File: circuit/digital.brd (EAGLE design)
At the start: 56.2 x 50.8 mm, 24 parts, among them IC1 MCP1701-5V, IC2 MCP1700-3.3V, X1 MINI-USB-SCHIELD-32005-301

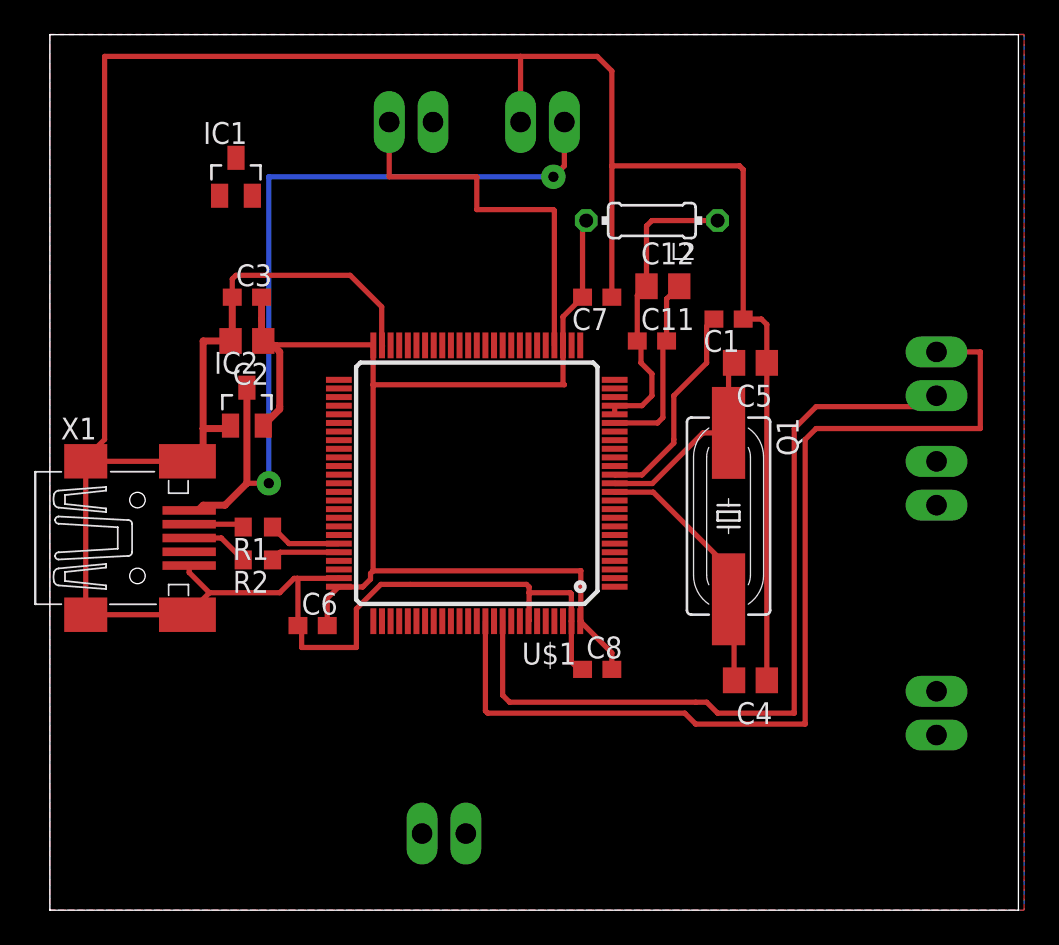
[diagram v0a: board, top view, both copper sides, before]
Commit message: - развели все пины идущие к аналоговой части
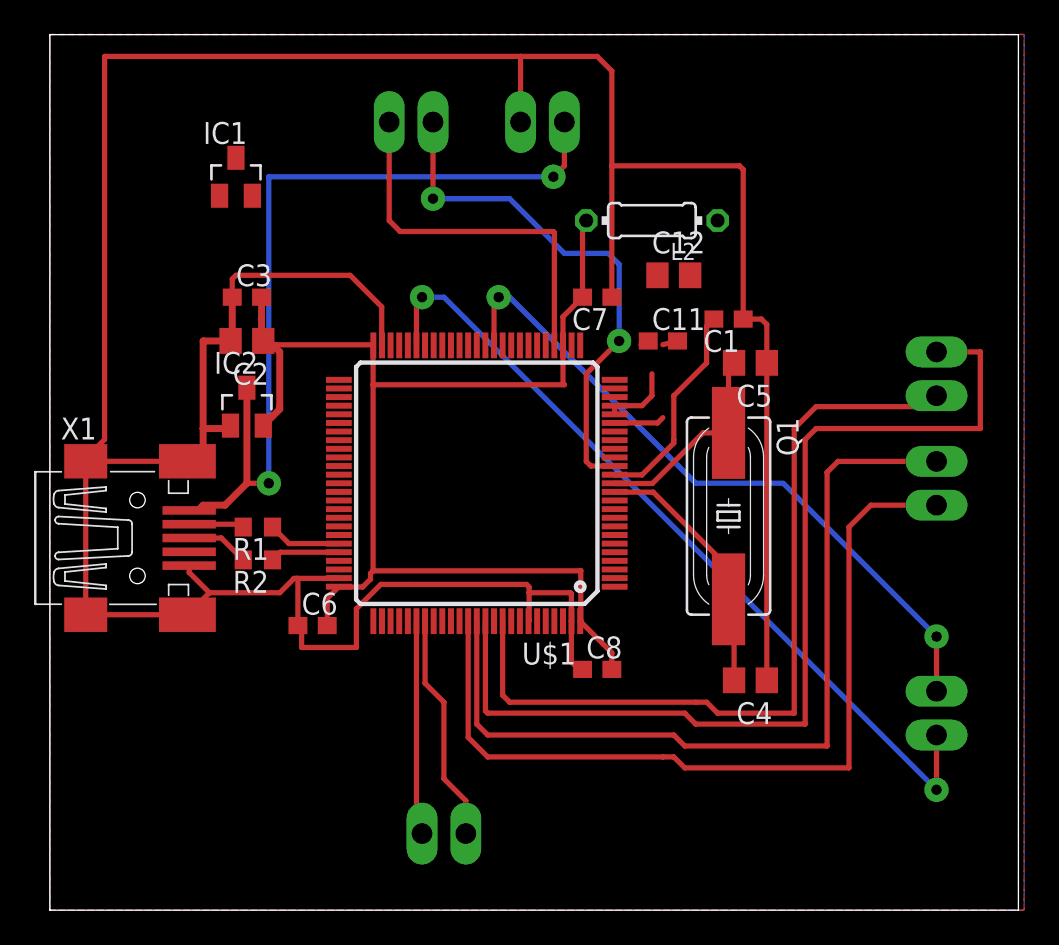
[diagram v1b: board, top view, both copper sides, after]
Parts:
- moved C12 0.90 mm to (36.2, 36.8)
- moved C11 0.64 mm to (35.6, 33.0)
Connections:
- net I_ADC: now also U$1.45; no longer U$1.36
- net RA: now also U$1.82
- net RB: now also U$1.81
- net SPI_CS_I: now also U$1.87
- net SPI_CS_V: now also U$1.88
- net V_ADC: now also U$1.36; no longer U$1.45
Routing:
- net SPI_CS_V: track 0.00 -> 49.3 mm
- net SPI_CS_I: track 0.00 -> 49.1 mm
- net I_ADC: track 0.00 -> 47.8 mm, vias 0 -> 2
- net V_ADC: track 0.00 -> 39.6 mm, vias 0 -> 2
- net ADC12_IN6: track 0.00 -> 30.8 mm, vias 0 -> 2
- net RA: track 0.00 -> 13.3 mm
- net V+: track 17.6 -> 4.64 mm
- net RB: track 0.00 -> 12.5 mm
- net GNDA: track 10.9 -> 3.80 mm
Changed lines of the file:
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@@
 <elements>
 <element name="L2" library="rcl" package="0204/7" value="MMZ1608B102C" x="34.925" y="40.005" rot="R180"/>
-<element name="C11" library="rcl" package="C0603" value="100n" x="34.925" y="33.02"/>
-<element name="C12" library="rcl" package="C0805" value="10mk" x="35.56" y="36.195"/>
+<element name="C11" library="rcl" package="C0603" value="100n" x="35.56" y="33.02"/>
+<element name="C12" library="rcl" package="C0805" value="10mk" x="36.195" y="36.83"/>
 <element name="X2" library="con-phoenix-254" package="2POL254" value="" x="28.575" y="45.72" rot="MR0">
 <attribute name="OC_NEWARK" value="unknown" x="-19.685" y="5.08" size="1.778" layer="28" rot="MR0" display="off"/>
@@
 <contactref element="X8" pad="1"/>
 <contactref element="U$1" pad="29"/>
-<wire x1="29.265" y1="32.765" x2="29.265" y2="40.585" width="0.3048" layer="1"/>
-<wire x1="29.265" y1="40.585" x2="29.21" y2="40.64" width="0.3048" layer="1"/>
-<wire x1="29.21" y1="40.64" x2="24.765" y2="40.64" width="0.3048" layer="1"/>
-<wire x1="19.685" y1="45.72" x2="19.685" y2="42.545" width="0.3048" layer="1"/>
-<wire x1="19.685" y1="42.545" x2="24.765" y2="42.545" width="0.3048" layer="1"/>
-<wire x1="24.765" y1="42.545" x2="24.765" y2="40.64" width="0.3048" layer="1"/>
+<wire x1="29.265" y1="32.765" x2="29.265" y2="39.315" width="0.3048" layer="1"/>
+<wire x1="29.265" y1="39.315" x2="29.21" y2="39.37" width="0.3048" layer="1"/>
+<wire x1="29.21" y1="39.37" x2="20.32" y2="39.37" width="0.3048" layer="1"/>
+<wire x1="20.32" y1="39.37" x2="19.685" y2="40.005" width="0.3048" layer="1"/>
+<wire x1="19.685" y1="40.005" x2="19.685" y2="45.72" width="0.3048" layer="1"/>
 </signal>
 <signal name="+5V">
@@
 <wire x1="32.765" y1="28.265" x2="35.25" y2="28.265" width="0.3048" layer="1"/>
 <wire x1="35.25" y1="28.265" x2="35.56" y2="28.575" width="0.3048" layer="1"/>
-<wire x1="35.56" y1="28.575" x2="35.56" y2="32.805" width="0.3048" layer="1"/>
-<wire x1="35.56" y1="32.805" x2="35.775" y2="33.02" width="0.3048" layer="1"/>
-<wire x1="35.775" y1="33.02" x2="35.775" y2="35.46" width="0.3048" layer="1"/>
-<wire x1="35.775" y1="35.46" x2="36.51" y2="36.195" width="0.3048" layer="1"/>
+<wire x1="35.56" y1="28.575" x2="35.56" y2="32.805" width="0" layer="19" extent="1-16"/>
+<wire x1="35.56" y1="32.805" x2="36.41" y2="33.02" width="0.3048" layer="1"/>
+<wire x1="36.41" y1="33.02" x2="35.775" y2="35.46" width="0" layer="19" extent="1-16"/>
+<wire x1="35.775" y1="35.46" x2="37.145" y2="36.83" width="0" layer="19" extent="1-16"/>
 </signal>
 <signal name="V_ADC">
 <contactref element="X5" pad="1"/>
-<contactref element="U$1" pad="45"/>
-<wire x1="21.265" y1="32.765" x2="51.435" y2="12.7" width="0" layer="19" extent="1-1"/>
+<contactref element="U$1" pad="36"/>
+<wire x1="25.765" y1="32.765" x2="25.765" y2="35.29" width="0.3048" layer="1"/>
+<wire x1="25.765" y1="35.29" x2="26.035" y2="35.56" width="0.3048" layer="1"/>
+<via x="26.035" y="35.56" extent="1-16" drill="0.6" diameter="1.4224" shape="square"/>
+<via x="51.435" y="15.875" extent="1-16" drill="0.6" diameter="1.4224" shape="square"/>
+<wire x1="51.435" y1="15.875" x2="51.435" y2="12.7" width="0.3048" layer="1"/>
+<wire x1="26.035" y1="35.56" x2="26.67" y2="35.56" width="0.3048" layer="16"/>
+<wire x1="26.67" y1="35.56" x2="37.465" y2="24.765" width="0.3048" layer="16"/>
+<wire x1="37.465" y1="24.765" x2="42.545" y2="24.765" width="0.3048" layer="16"/>
+<wire x1="42.545" y1="24.765" x2="51.435" y2="15.875" width="0.3048" layer="16"/>
 </signal>
 <signal name="RA">
 <contactref element="X4" pad="1"/>
+<contactref element="U$1" pad="82"/>
+<wire x1="21.765" y1="16.765" x2="21.765" y2="13.16" width="0.3048" layer="1"/>
+<wire x1="21.765" y1="13.16" x2="22.86" y2="12.065" width="0.3048" layer="1"/>
+<wire x1="22.86" y1="12.065" x2="22.86" y2="7.62" width="0.3048" layer="1"/>
+<wire x1="22.86" y1="7.62" x2="24.13" y2="6.35" width="0.3048" layer="1"/>
+<wire x1="24.13" y1="6.35" x2="24.13" y2="4.445" width="0.3048" layer="1"/>
 </signal>
 <signal name="RB">
 <contactref element="X4" pad="2"/>
-<wire x1="18.9484" y1="4.445" x2="21.59" y2="4.445" width="0" layer="19" extent="1-16"/>
+<contactref element="U$1" pad="81"/>
+<wire x1="21.265" y1="16.765" x2="21.265" y2="4.77" width="0.3048" layer="1"/>
+<wire x1="21.265" y1="4.77" x2="21.59" y2="4.445" width="0.3048" layer="1"/>
 </signal>
 <signal name="SPI_CS_I">
 <contactref element="X7" pad="2"/>
+<contactref element="U$1" pad="87"/>
+<wire x1="24.265" y1="16.765" x2="24.265" y2="10.025" width="0.3048" layer="1"/>
+<wire x1="24.265" y1="10.025" x2="25.4" y2="8.89" width="0.3048" layer="1"/>
+<wire x1="25.4" y1="8.89" x2="35.56" y2="8.89" width="0.3048" layer="1"/>
+<wire x1="35.56" y1="8.89" x2="36.195" y2="8.89" width="0.3048" layer="1"/>
+<wire x1="36.195" y1="8.89" x2="36.83" y2="8.255" width="0.3048" layer="1"/>
+<wire x1="36.83" y1="8.255" x2="46.355" y2="8.255" width="0.3048" layer="1"/>
+<wire x1="46.355" y1="8.255" x2="46.355" y2="22.225" width="0.3048" layer="1"/>
+<wire x1="46.355" y1="22.225" x2="47.625" y2="23.495" width="0.3048" layer="1"/>
+<wire x1="47.625" y1="23.495" x2="51.435" y2="23.495" width="0.3048" layer="1"/>
 </signal>
 <signal name="I_ADC">
 <contactref element="X5" pad="2"/>
-<contactref element="U$1" pad="36"/>
-<wire x1="25.765" y1="32.765" x2="51.435" y2="10.16" width="0" layer="19" extent="1-1"/>
+<contactref element="U$1" pad="45"/>
+<wire x1="21.265" y1="32.765" x2="21.265" y2="35.235" width="0.3048" layer="1"/>
+<wire x1="21.265" y1="35.235" x2="21.59" y2="35.56" width="0.3048" layer="1"/>
+<via x="21.59" y="35.56" extent="1-16" drill="0.6" diameter="1.4224" shape="square"/>
+<wire x1="21.59" y1="35.56" x2="22.86" y2="35.56" width="0.3048" layer="16"/>
+<wire x1="22.86" y1="35.56" x2="51.435" y2="6.985" width="0.3048" layer="16"/>
+<via x="51.435" y="6.985" extent="1-16" drill="0.6" diameter="1.4224" shape="square"/>
+<wire x1="51.435" y1="6.985" x2="51.435" y2="10.16" width="0.3048" layer="1"/>
 </signal>
 <signal name="SPI_CS_V">
 <contactref element="X7" pad="1"/>
+<contactref element="U$1" pad="88"/>
+<wire x1="24.765" y1="16.765" x2="24.765" y2="10.795" width="0.3048" layer="1"/>
+<wire x1="24.765" y1="10.795" x2="25.4" y2="10.16" width="0.3048" layer="1"/>
+<wire x1="25.4" y1="10.16" x2="36.195" y2="10.16" width="0.3048" layer="1"/>
+<wire x1="36.195" y1="10.16" x2="36.83" y2="9.525" width="0.3048" layer="1"/>
+<wire x1="36.83" y1="9.525" x2="45.085" y2="9.525" width="0.3048" layer="1"/>
+<wire x1="45.085" y1="9.525" x2="45.085" y2="25.4" width="0.3048" layer="1"/>
+<wire x1="45.085" y1="25.4" x2="45.72" y2="26.035" width="0.3048" layer="1"/>
+<wire x1="45.72" y1="26.035" x2="51.435" y2="26.035" width="0.3048" layer="1"/>
 </signal>
 <signal name="N$1">
@@
 <wire x1="34.345" y1="29.265" x2="34.925" y2="29.845" width="0.3048" layer="1"/>
 <wire x1="34.925" y1="29.845" x2="34.925" y2="31.115" width="0.3048" layer="1"/>
-<wire x1="34.925" y1="31.115" x2="34.29" y2="31.75" width="0.3048" layer="1"/>
-<wire x1="34.29" y1="31.75" x2="34.29" y2="32.805" width="0.3048" layer="1"/>
-<wire x1="34.29" y1="32.805" x2="34.075" y2="33.02" width="0.3048" layer="1"/>
-<wire x1="34.075" y1="33.02" x2="34.075" y2="35.66" width="0.3048" layer="1"/>
-<wire x1="34.075" y1="35.66" x2="34.61" y2="36.195" width="0.3048" layer="1"/>
-<wire x1="34.61" y1="36.195" x2="34.61" y2="39.69" width="0.3048" layer="1"/>
-<wire x1="34.61" y1="39.69" x2="34.925" y2="40.005" width="0.3048" layer="1"/>
-<wire x1="34.925" y1="40.005" x2="38.735" y2="40.005" width="0.3048" layer="1"/>
+<wire x1="34.925" y1="31.115" x2="34.29" y2="31.75" width="0" layer="19" extent="1-16"/>
+<wire x1="34.29" y1="31.75" x2="34.29" y2="32.805" width="0" layer="19" extent="1-16"/>
+<wire x1="34.29" y1="32.805" x2="34.71" y2="33.02" width="0.3048" layer="1"/>
+<wire x1="34.71" y1="33.02" x2="34.075" y2="35.66" width="0" layer="19" extent="1-16"/>
+<wire x1="34.075" y1="35.66" x2="35.245" y2="36.83" width="0" layer="19" extent="1-16"/>
+<wire x1="35.245" y1="36.83" x2="34.61" y2="39.69" width="0" layer="19" extent="1-16"/>
+<wire x1="34.61" y1="39.69" x2="34.925" y2="40.005" width="0" layer="19" extent="1-16"/>
+<wire x1="34.925" y1="40.005" x2="38.735" y2="40.005" width="0" layer="19" extent="1-16"/>
 </signal>
 <signal name="N$4">
@@
 <contactref element="U$1" pad="15"/>
 <contactref element="X8" pad="2"/>
-<wire x1="32.765" y1="25.765" x2="22.225" y2="45.72" width="0" layer="19" extent="1-1"/>
+<wire x1="32.765" y1="25.765" x2="31.385" y2="25.765" width="0.3048" layer="1"/>
+<wire x1="31.385" y1="25.765" x2="31.115" y2="26.035" width="0.3048" layer="1"/>
+<wire x1="31.115" y1="26.035" x2="31.115" y2="31.115" width="0.3048" layer="1"/>
+<wire x1="31.115" y1="31.115" x2="33.02" y2="33.02" width="0.3048" layer="1"/>
+<via x="33.02" y="33.02" extent="1-16" drill="0.6" diameter="1.4224" shape="square"/>
+<via x="22.225" y="41.275" extent="1-16" drill="0.6" diameter="1.4224" shape="square"/>
+<wire x1="22.225" y1="41.275" x2="22.225" y2="45.72" width="0.3048" layer="1"/>
+<wire x1="33.02" y1="33.02" x2="33.02" y2="37.465" width="0.3048" layer="16"/>
+<wire x1="33.02" y1="37.465" x2="32.385" y2="38.1" width="0.3048" layer="16"/>
+<wire x1="32.385" y1="38.1" x2="29.845" y2="38.1" width="0.3048" layer="16"/>
+<wire x1="29.845" y1="38.1" x2="26.67" y2="41.275" width="0.3048" layer="16"/>
+<wire x1="26.67" y1="41.275" x2="22.225" y2="41.275" width="0.3048" layer="16"/>
 </signal>
 </signals>

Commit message: - все кроме LCD дисплея
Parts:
- added C10, C9: 1mk, rcl:C0603
- added R3: 0, rcl:R0603
- added X3: (no value), con-phoenix-254:2POL254
- moved IC1 1.42 mm to (10.2, 41.3), turned to 90 degrees
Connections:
- new net N$7: C9.1, IC1.3, X3.1
- net +5V: now also C10.1, IC1.2
- net GND: now also C10.2, C9.2, IC1.1, R3.2, X3.2
- net GNDA: now also R3.1
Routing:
- net +5V: track 48.5 -> 76.2 mm
- net GND: track 197.2 -> 216.5 mm
- net GNDA: track 3.80 -> 21.5 mm
- net V+: track 4.64 -> 17.1 mm
- net N$7: track 0.00 -> 7.75 mm

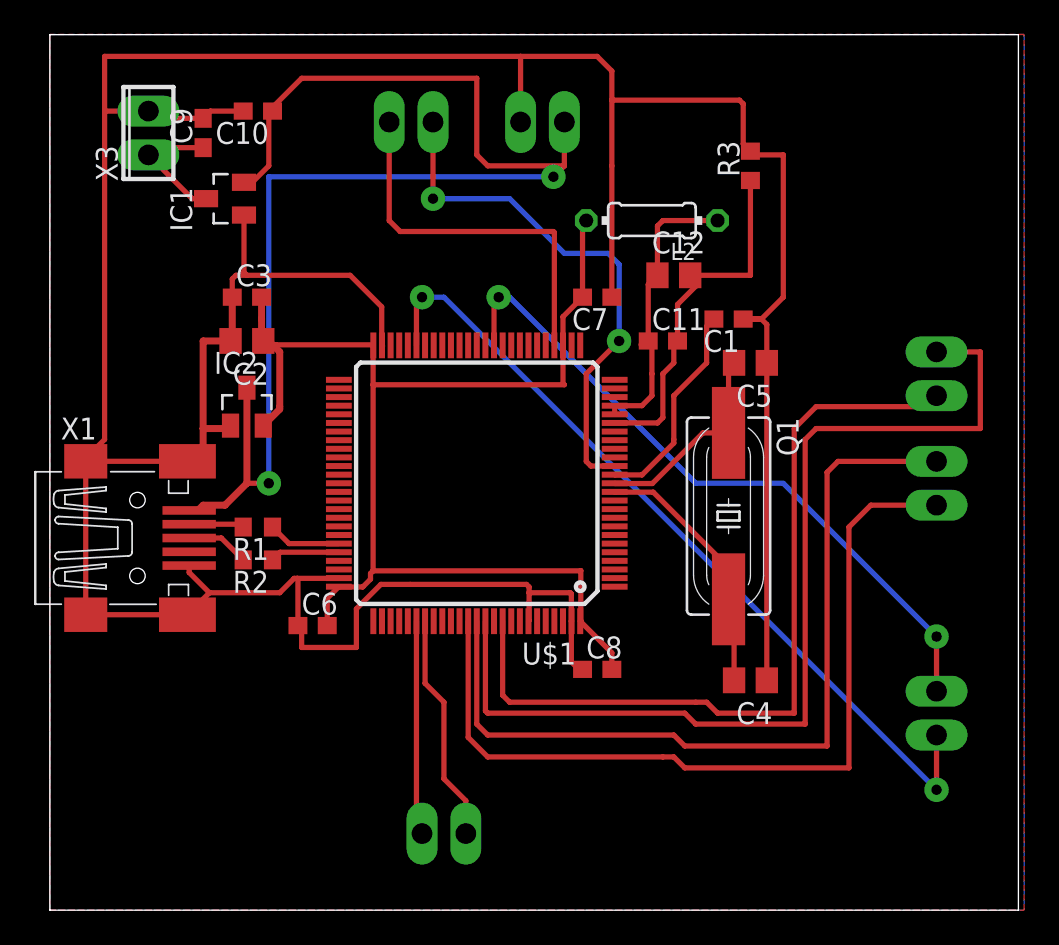
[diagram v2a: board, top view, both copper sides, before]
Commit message: - вывели 4 IO пина на всяк случай, для LCD
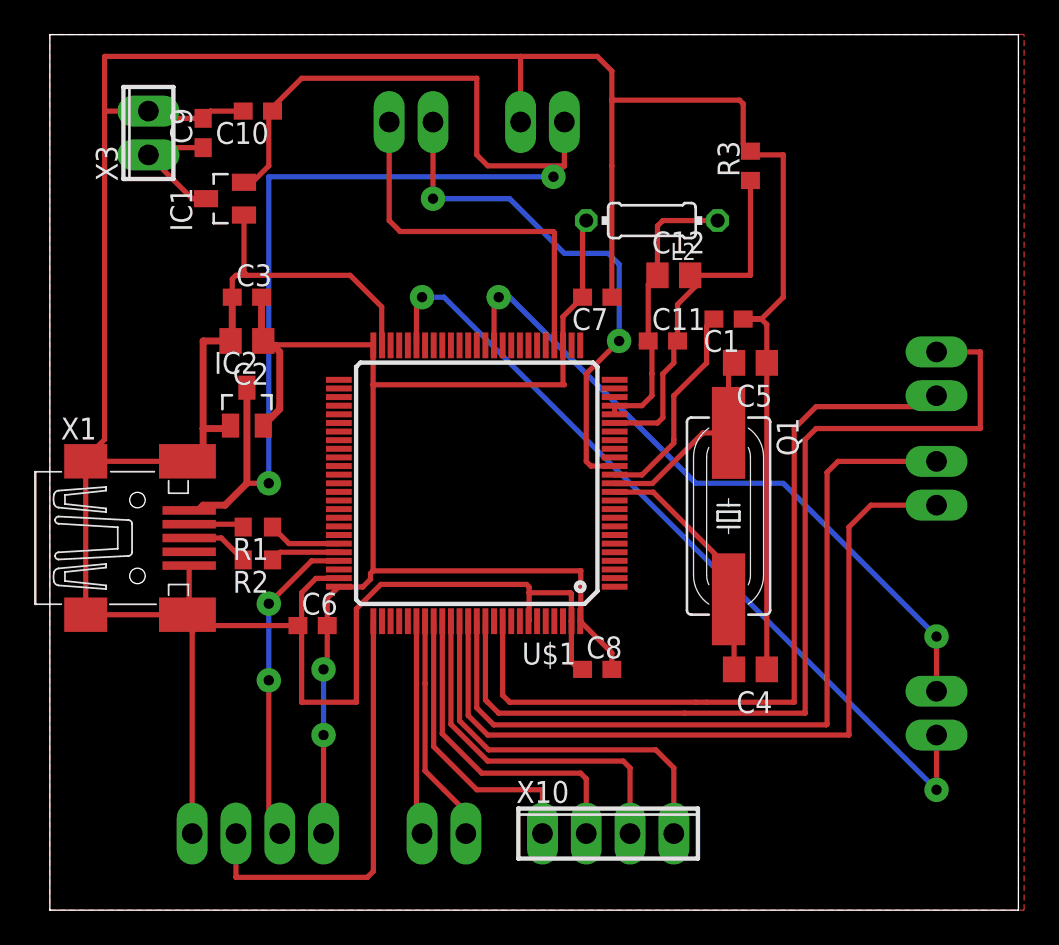
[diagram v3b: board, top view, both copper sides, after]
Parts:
- added X10, X9: (no value), con-phoenix-254:4POL254
- moved C4 0.63 mm to (40.6, 14.0)
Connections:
- new net N$10: U$1.86, X10.4
- new net N$6: U$1.83, X10.1
- new net N$8: U$1.84, X10.2
- new net N$9: U$1.85, X10.3
- new net SWCLK: U$1.76, X9.3
- new net SWDIO: U$1.72, X9.2
- net +3V3: now also X9.1
- net GND: now also X9.4
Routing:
- net SWCLK: track 0.00 -> 25.2 mm
- net N$10: track 0.00 -> 23.2 mm
- net N$9: track 0.00 -> 21.2 mm
- net N$8: track 0.00 -> 19.1 mm
- net SWDIO: track 0.00 -> 18.7 mm, vias 0 -> 2
- net GND: track 216.5 -> 234.0 mm
- net N$6: track 0.00 -> 17.2 mm
- net +3V3: track 72.2 -> 84.4 mm, vias 0 -> 2
- net SPI_CS_I: track 49.1 -> 45.7 mm
- net SPI_CS_V: track 49.3 -> 47.0 mm
- net SPI1_SCK: track 58.0 -> 56.7 mm
- net SPI1_MOSI: track 47.2 -> 46.3 mm
- removed copper zone on layer 16, net GNDA
